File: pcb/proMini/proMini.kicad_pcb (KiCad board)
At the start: 2 copper layers, 10 parts

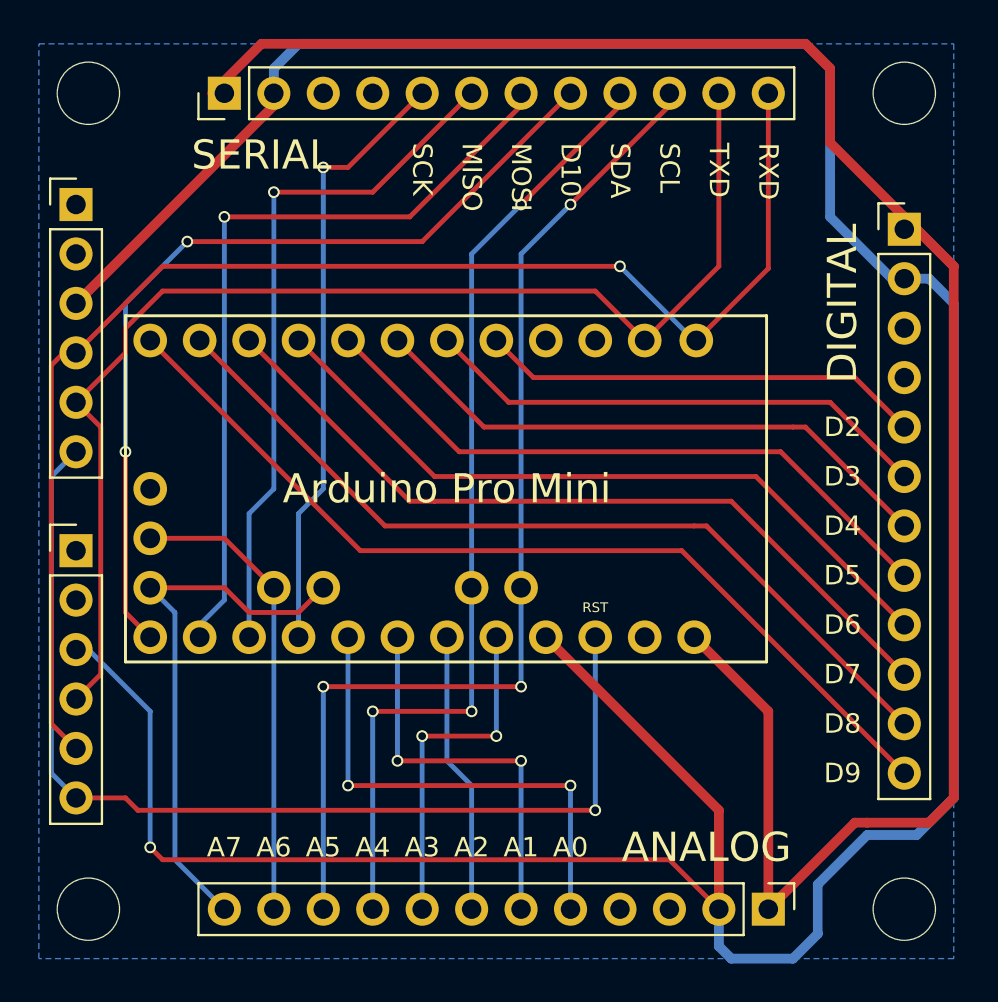
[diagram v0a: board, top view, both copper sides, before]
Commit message: Added a Rotary Encoder module. Tidied up a couple of modules before printing them.
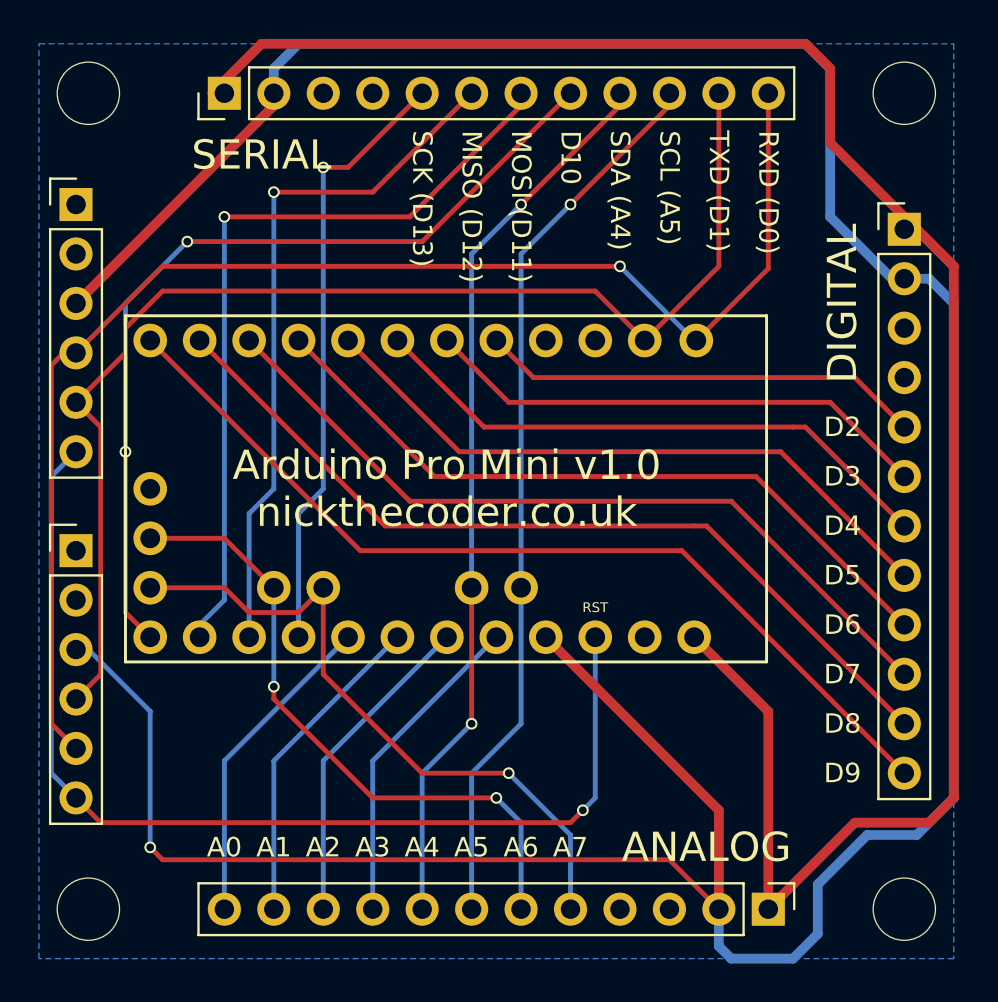
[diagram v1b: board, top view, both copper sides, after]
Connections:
- O3 pad 10: /A5 -> /A2
- O3 pad 11: /A6 -> /A1
- O3 pad 12: /A7 -> /A0
- O3 pad 5: /A0 -> /A7
- O3 pad 6: /A1 -> /A6
- O3 pad 7: /A2 -> /A5
- O3 pad 8: /A3 -> /A4
- O3 pad 9: /A4 -> /A3
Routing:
- net /A5: track 55.2 -> 46.1 mm, vias 3 -> 1
- net /A6: track 23.9 -> 32.9 mm, vias 0 -> 2
- net /A0: track 25.4 -> 16.6 mm, vias 2 -> 0
- net /A7: track 28.0 -> 34.3 mm, vias 0 -> 1
- net /A4: track 50.1 -> 46.1 mm, vias 3 -> 2
- net /A1: track 20.3 -> 16.6 mm, vias 2 -> 0
- net /A2: track 14.5 -> 16.6 mm
- net /A3: track 17.8 -> 16.6 mm, vias 2 -> 0
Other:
- board text added: "Arduino Pro Mini v1.0 nickthecoder.co.uk"
- board text added: "MISO (D12)"
- board text added: "MOSI (D11)"
- board text added: "RXD (D0)"
- board text added: "SCK (D13)"
- board text added: "SCL (A5)"
- board text added: "SDA (A4)"
- board text added: "TXD (D1)"
- board text removed: "Arduino Pro Mini"
- board text removed: "MISO"
- board text removed: "MOSI"
- board text removed: "RXD"
- board text removed: "SCK"
- board text removed: "SCL"
- board text removed: "SDA"
- board text removed: "TXD"
